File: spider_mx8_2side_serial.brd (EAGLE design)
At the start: 18.7 x 52.9 mm, 7 parts, among them J1 AVR_SPI_PRG_6NS

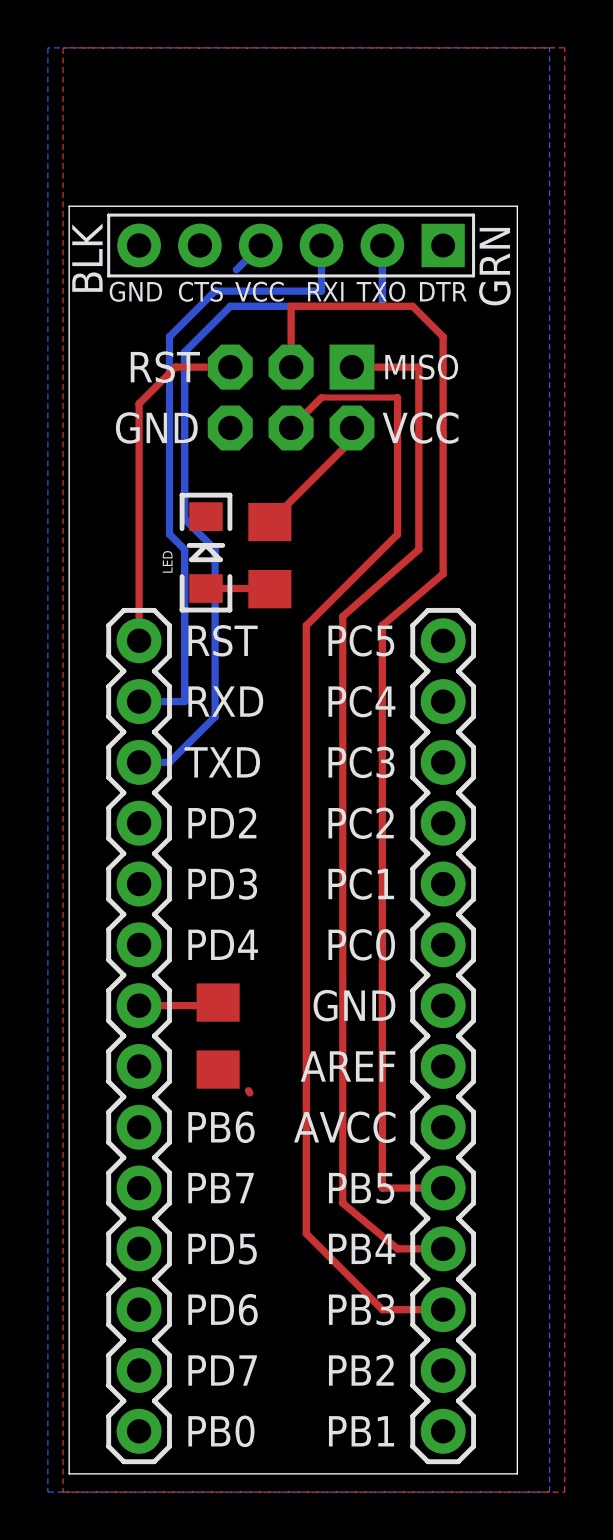
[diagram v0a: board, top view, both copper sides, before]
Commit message: added power jumper to serial: mx8 spider
other tweaks include stuff with the 8LED modules
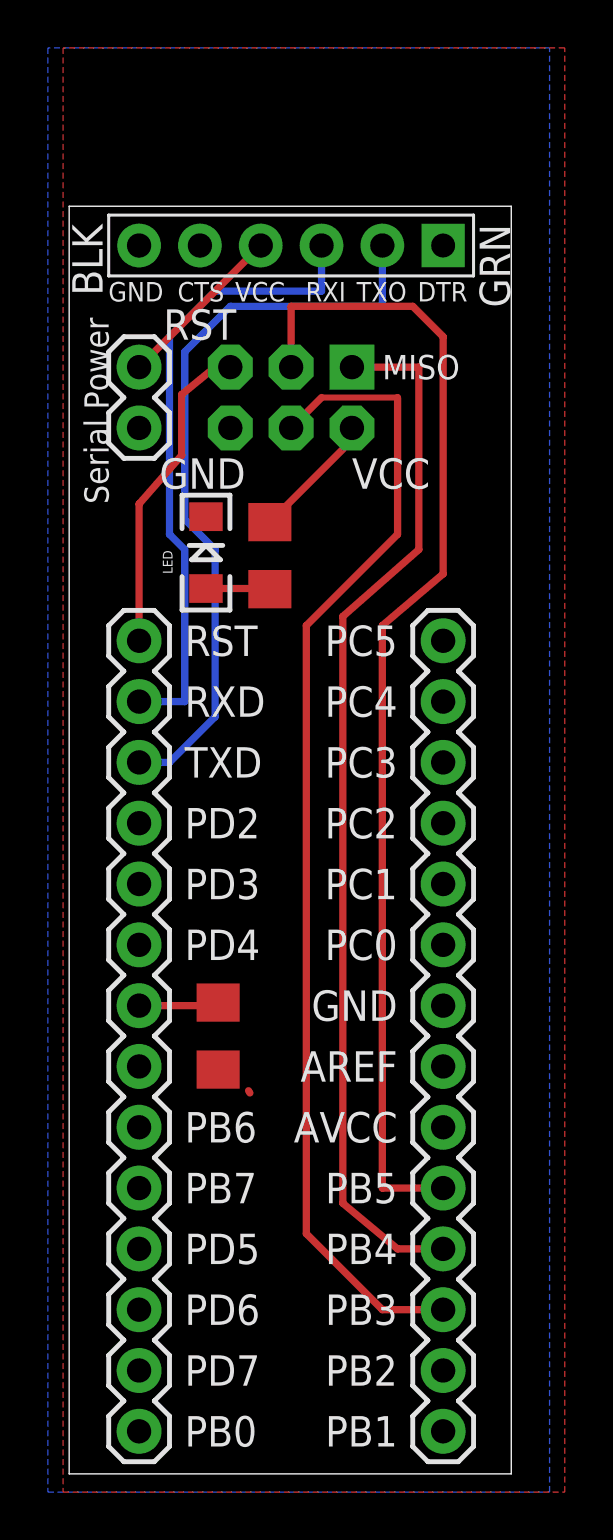
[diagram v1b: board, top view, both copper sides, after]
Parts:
- added SERIAL_POWER: M02PTH, SparkFun-Connectors:1X02
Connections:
- new net VCC_SERIAL: JP2.P$4, SERIAL_POWER.1
- net VCC: now also SERIAL_POWER.2; no longer JP2.P$4
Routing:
- net VCC_SERIAL: track 0.00 -> 7.18 mm
- net VCC: track 10.2 -> 8.79 mm
- net RESET: track 14.3 -> 13.4 mm
- net GND: track 0.80 -> 1.35 mm
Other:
- board size 18.7 x 52.9 mm -> 18.5 x 52.9 mm
- board text added: "Serial Power"
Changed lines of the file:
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@@
 <board>
 <plain>
-<wire x1="33.909" y1="18.542" x2="52.629" y2="18.542" width="0" layer="20"/>
-<wire x1="52.629" y1="18.542" x2="52.629" y2="71.491" width="0" layer="20"/>
-<wire x1="52.629" y1="71.491" x2="33.909" y2="71.491" width="0" layer="20"/>
+<wire x1="33.909" y1="18.542" x2="52.375" y2="18.542" width="0" layer="20"/>
+<wire x1="52.375" y1="18.542" x2="52.375" y2="71.491" width="0" layer="20"/>
+<wire x1="52.375" y1="71.491" x2="33.909" y2="71.491" width="0" layer="20"/>
 <wire x1="33.909" y1="71.491" x2="33.909" y2="18.542" width="0" layer="20"/>
 <text x="38.735" y="53.34" size="1.27" layer="25" align="center-left">RST</text>
@@
 <text x="47.625" y="22.86" size="1.27" layer="25" align="center-right">PB2</text>
 <text x="47.625" y="20.32" size="1.27" layer="25" align="center-right">PB1</text>
-<text x="39.37" y="64.77" size="1.27" layer="25" align="center-right">RST</text>
-<text x="39.37" y="62.23" size="1.27" layer="25" align="center-right">GND</text>
+<text x="37.846" y="66.548" size="1.27" layer="25" rot="R180" align="center-right">RST</text>
+<text x="41.275" y="60.325" size="1.27" layer="25" align="center-right">GND</text>
 <text x="46.99" y="64.77" size="1.016" layer="25" align="center-left">MISO</text>
-<text x="46.99" y="62.23" size="1.27" layer="25" align="center-left">VCC</text>
+<text x="45.72" y="60.325" size="1.27" layer="25" align="center-left">VCC</text>
 <text x="43.18" y="53.975" size="1.27" layer="26" rot="MR270" align="center-left">Mega xx8 Programming Spider
 Version 1.0</text>
+<text x="35.56" y="59.055" size="1.016" layer="25" rot="R90">Serial Power</text>
 </plain>
 <attributes>
@@
 <element name="JP1" library="SparkFun-Connectors" package="1X14" value="M14" x="36.83" y="20.32" smashed="yes" rot="R90"/>
 <element name="JP2" library="SparkFun-Connectors" package="FTDI_DEVICE_SIDE" value="FTDI_DEVICE" x="43.18" y="69.85" smashed="yes" rot="R180"/>
+<element name="SERIAL_POWER" library="SparkFun-Connectors" package="1X02" value="M02PTH" x="36.83" y="64.77" smashed="yes" rot="R270"/>
 </elements>
 <signals>
@@
 <signal name="RESET">
 <contactref element="J1" pad="5"/>
-<wire x1="40.64" y1="64.77" x2="38.354" y2="64.77" width="0.3048" layer="1"/>
 <contactref element="JP1" pad="14"/>
-<wire x1="36.83" y1="63.246" x2="36.83" y2="53.34" width="0.3048" layer="1"/>
-<wire x1="38.354" y1="64.77" x2="36.83" y2="63.246" width="0.3048" layer="1"/>
+<wire x1="36.83" y1="59.055" x2="36.83" y2="53.34" width="0.3048" layer="1"/>
+<wire x1="38.608" y1="61.087" x2="36.83" y2="59.055" width="0.3048" layer="1"/>
+<wire x1="38.608" y1="61.087" x2="38.608" y2="63.627" width="0.3048" layer="1"/>
+<wire x1="38.608" y1="63.627" x2="40.005" y2="64.77" width="0.3048" layer="1"/>
+<wire x1="40.005" y1="64.77" x2="40.64" y2="64.77" width="0.3048" layer="1"/>
 </signal>
 <signal name="VCC">
@@
 <wire x1="45.72" y1="61.722" x2="42.418" y2="58.42" width="0.3048" layer="1"/>
 <wire x1="45.72" y1="62.23" x2="45.72" y2="61.722" width="0.3048" layer="1"/>
-<contactref element="JP2" pad="P$4"/>
-<wire x1="40.894" y1="68.834" x2="41.91" y2="69.85" width="0.3048" layer="16"/>
 <wire x1="42.418" y1="58.42" x2="42.415" y2="58.42" width="0.3048" layer="1"/>
 <wire x1="42.415" y1="58.42" x2="42.291" y2="58.296" width="0.3048" layer="1"/>
+<contactref element="SERIAL_POWER" pad="2"/>
 </signal>
 <signal name="GND">
@@
 <wire x1="39.878" y1="35.814" x2="39.979603125" y2="35.814" width="0.3048" layer="1"/>
 <contactref element="JP2" pad="P$6"/>
+<wire x1="39.624" y1="58.674" x2="39.624" y2="58.523" width="0.3048" layer="1"/>
+<wire x1="39.878" y1="58.674" x2="39.624" y2="58.523" width="0.3048" layer="1"/>
+<wire x1="39.878" y1="58.674" x2="39.77161875" y2="58.6706" width="0.3048" layer="1"/>
 </signal>
 <signal name="N$14">
@@
 <wire x1="38.1" y1="57.785" x2="38.1" y2="66.04" width="0.3048" layer="16"/>
 </signal>
+<signal name="VCC_SERIAL">
+<contactref element="JP2" pad="P$4"/>
+<contactref element="SERIAL_POWER" pad="1"/>
+<wire x1="36.83" y1="64.77" x2="41.402" y2="69.342" width="0.3048" layer="1"/>
+<wire x1="41.402" y1="69.342" x2="41.91" y2="69.85" width="0.254" layer="1"/>
+</signal>
 </signals>
